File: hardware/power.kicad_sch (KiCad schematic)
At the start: 34 parts, among them U3 TI LMR51430YFDDCR, U4 TI LMR51430YFDDCR, U5 TPS2116DRLR, U6 NCV8187AMT180TAG, U7 LP5912-3.3DRVR

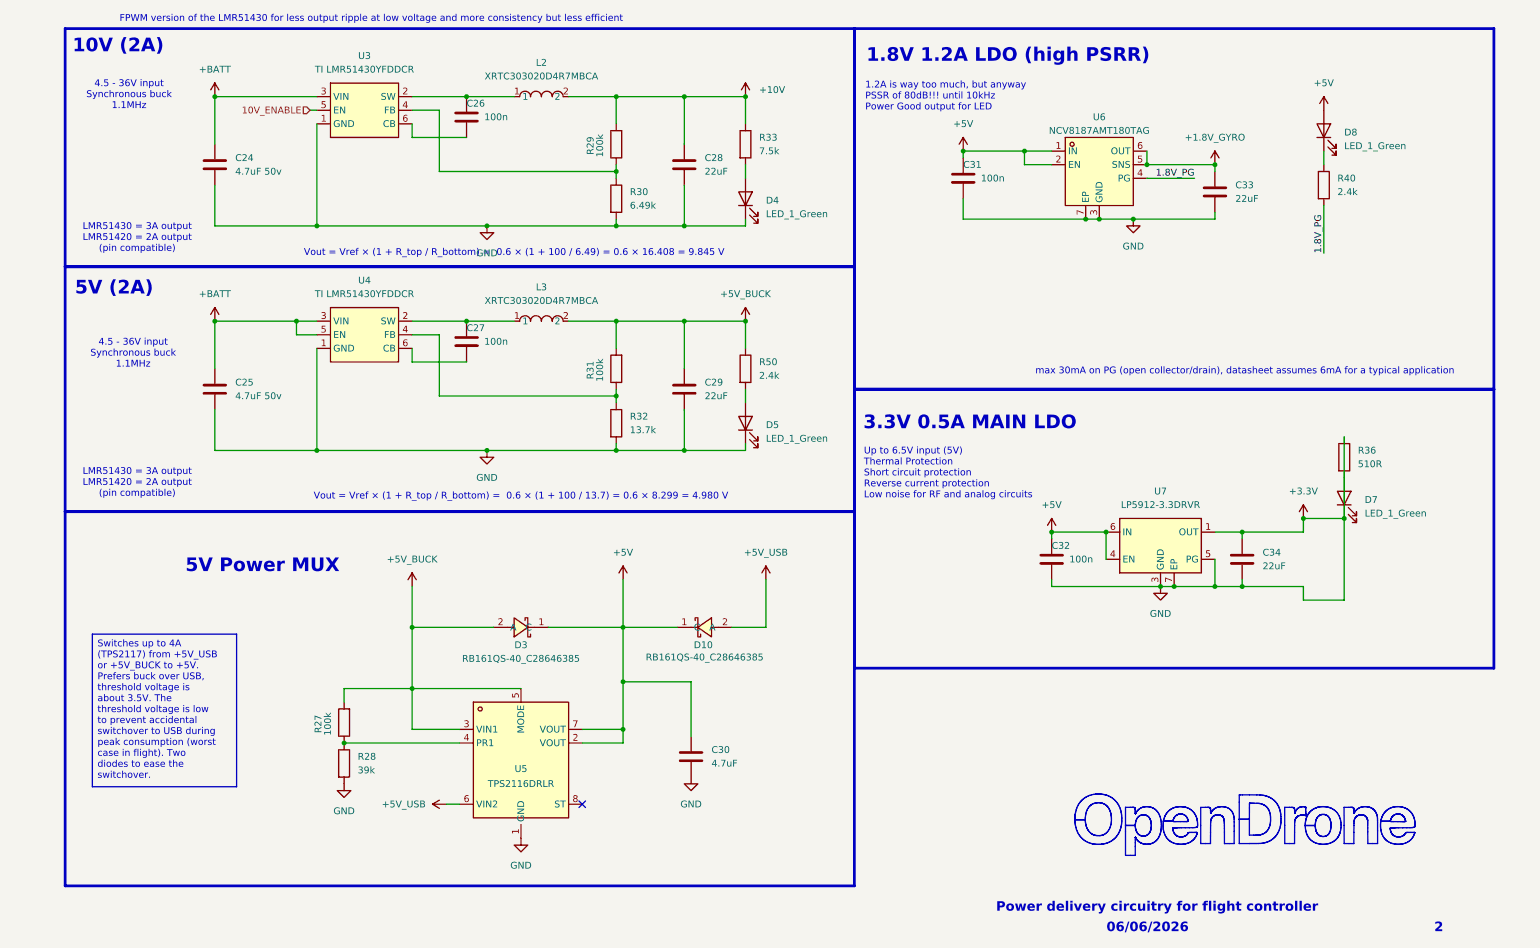
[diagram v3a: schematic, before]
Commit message: fix(power): break accidental +3.3V↔GND short in power sheet
A +3.3V power symbol (#PWR084) and a GND symbol (#PWR068) were tied to the same
net during schematic annotation, merging the entire ground into +3.3V (no GND
net, 14 shorted caps, LDO IN/GND/OUT shorted). Separated them; ERC +3.3V/GND
conflict cleared, GND net restored (91 pins), 0 shorted caps. PCB unaffected.

Co-Authored-By: Claude Opus 4.8 (1M context) <noreply@anthropic.com>
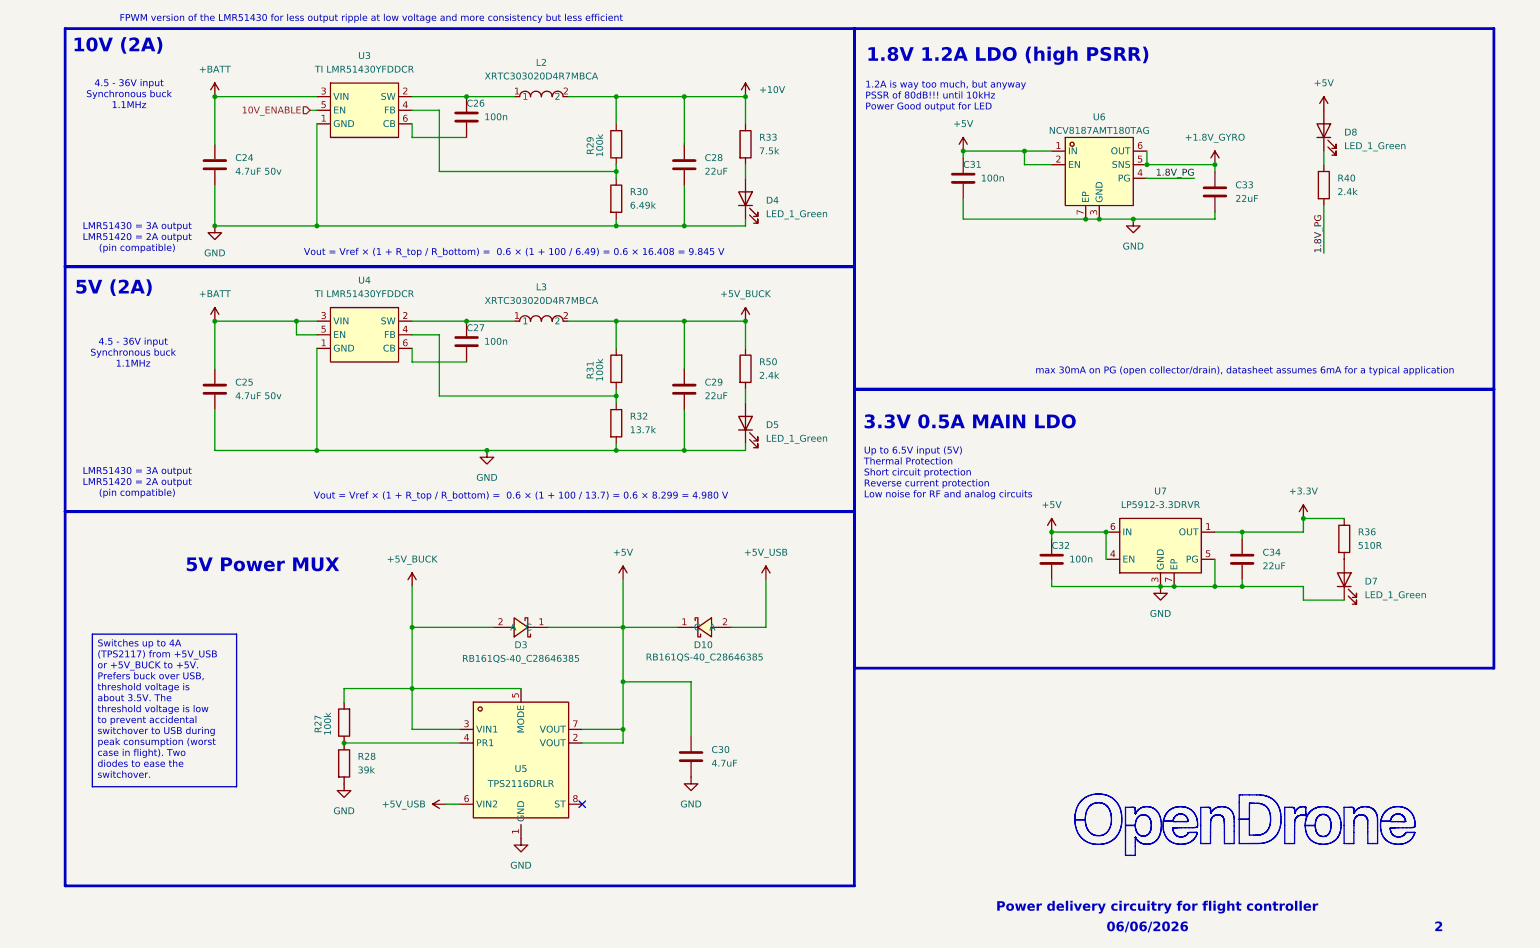
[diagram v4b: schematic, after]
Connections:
- net +3.3V: no longer C24.2, C25.2, C28.2, C29.2, C30.2, C31.2, C32.2, C33.2, C34.2, D4.1 (K), D5.1 (K), D7.1 (K), R28.2, R30.2, R32.2, U3.1 (GND), U4.1 (GND), U5.1 (GND), U6.3 (GND), U6.7 (EP), U7.3 (GND), U7.5 (PG), U7.7 (EP)
- new net GND: C24.2, C25.2, C28.2, C29.2, C30.2, C31.2, C32.2, C33.2, C34.2, D4.1 (K), D5.1 (K), D7.1 (K), R28.2, R30.2, R32.2, U3.1 (GND), U4.1 (GND), U5.1 (GND), U6.3 (GND), U6.7 (EP), U7.3 (GND), U7.5 (PG), U7.7 (EP)
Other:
- moved on the sheet: D7, R36
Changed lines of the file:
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@@
 	)
 	(junction
-		(at 198.12 119.38)
+		(at 245.11 116.84)
 		(diameter 0)
 		(color 0 0 0 0)
 	)
 	(junction
-		(at 245.11 116.84)
+		(at 198.12 119.38)
 		(diameter 0)
 		(color 0 0 0 0)
@@
 	)
 	(junction
-		(at 252.73 116.84)
-		(diameter 0)
-		(color 0 0 0 0)
-	)
-	(junction
 		(at 116.84 104.14)
 		(diameter 0)
@@
 	)
 	(junction
-		(at 118.11 137.16)
+		(at 41.91 62.23)
 		(diameter 0)
 		(color 0 0 0 0)
 	)
 	(junction
-		(at 140.97 38.1)
+		(at 118.11 137.16)
 		(diameter 0)
 		(color 0 0 0 0)
 	)
 	(junction
-		(at 92.71 62.23)
+		(at 140.97 38.1)
 		(diameter 0)
 		(color 0 0 0 0)
@@
 	(wire
 		(pts
-			(xy 213.36 60.96) (xy 228.6 60.96)
+			(xy 245.11 129.54) (xy 245.11 132.08)
 		)
 		(stroke
@@
 	(wire
 		(pts
-			(xy 116.84 80.01) (xy 116.84 85.09)
+			(xy 213.36 60.96) (xy 228.6 60.96)
 		)
 		(stroke
@@
 	(wire
 		(pts
-			(xy 140.97 60.96) (xy 140.97 62.23)
+			(xy 116.84 80.01) (xy 116.84 85.09)
 		)
 		(stroke
@@
 	(wire
 		(pts
-			(xy 218.44 129.54) (xy 220.98 129.54)
+			(xy 140.97 60.96) (xy 140.97 62.23)
 		)
 		(stroke
@@
 	(wire
 		(pts
-			(xy 181.61 48.26) (xy 193.04 48.26)
+			(xy 218.44 129.54) (xy 220.98 129.54)
 		)
 		(stroke
@@
 	(wire
 		(pts
-			(xy 193.04 48.26) (xy 198.12 48.26)
+			(xy 181.61 48.26) (xy 193.04 48.26)
 		)
 		(stroke
@@
 	(wire
 		(pts
-			(xy 110.49 158.75) (xy 118.11 158.75)
+			(xy 193.04 48.26) (xy 198.12 48.26)
 		)
 		(stroke
@@
 	(wire
 		(pts
-			(xy 207.01 60.96) (xy 213.36 60.96)
+			(xy 110.49 158.75) (xy 118.11 158.75)
 		)
 		(stroke
@@
 	(wire
 		(pts
-			(xy 116.84 62.23) (xy 92.71 62.23)
+			(xy 207.01 60.96) (xy 213.36 60.96)
 		)
 		(stroke
@@
 	(wire
 		(pts
-			(xy 60.96 62.23) (xy 41.91 62.23)
+			(xy 41.91 62.23) (xy 116.84 62.23)
 		)
 		(stroke
@@
 	(wire
 		(pts
-			(xy 78.74 148.59) (xy 78.74 156.21)
+			(xy 245.11 116.84) (xy 245.11 119.38)
 		)
 		(stroke
@@
 	(wire
 		(pts
-			(xy 78.74 40.64) (xy 83.82 40.64)
+			(xy 245.11 132.08) (xy 252.73 132.08)
 		)
 		(stroke
@@
 	(wire
 		(pts
-			(xy 41.91 80.01) (xy 41.91 88.9)
+			(xy 78.74 148.59) (xy 78.74 156.21)
 		)
 		(stroke
@@
 	(wire
 		(pts
-			(xy 92.71 104.14) (xy 60.96 104.14)
+			(xy 78.74 40.64) (xy 83.82 40.64)
 		)
 		(stroke
@@
 	(wire
 		(pts
-			(xy 233.68 129.54) (xy 228.6 129.54)
+			(xy 41.91 80.01) (xy 41.91 88.9)
 		)
 		(stroke
@@
 	(wire
 		(pts
-			(xy 92.71 62.23) (xy 60.96 62.23)
+			(xy 92.71 104.14) (xy 60.96 104.14)
 		)
 		(stroke
@@
 	(wire
 		(pts
-			(xy 85.09 170.18) (xy 87.63 170.18)
+			(xy 233.68 129.54) (xy 228.6 129.54)
 		)
 		(stroke
@@
 	(wire
 		(pts
-			(xy 198.12 119.38) (xy 208.28 119.38)
+			(xy 85.09 170.18) (xy 87.63 170.18)
 		)
 		(stroke
@@
 	(wire
 		(pts
-			(xy 116.84 80.01) (xy 129.54 80.01)
+			(xy 198.12 119.38) (xy 208.28 119.38)
 		)
 		(stroke
@@
 	(wire
 		(pts
-			(xy 83.82 82.55) (xy 83.82 93.98)
+			(xy 116.84 80.01) (xy 129.54 80.01)
 		)
 		(stroke
@@
 	(wire
 		(pts
-			(xy 193.04 48.26) (xy 193.04 50.8)
+			(xy 83.82 82.55) (xy 83.82 93.98)
 		)
 		(stroke
@@
 	(wire
 		(pts
-			(xy 78.74 129.54) (xy 78.74 137.16)
+			(xy 193.04 48.26) (xy 193.04 50.8)
 		)
 		(stroke
@@
 	(wire
 		(pts
-			(xy 228.6 124.46) (xy 228.6 129.54)
+			(xy 78.74 129.54) (xy 78.74 137.16)
 		)
 		(stroke
@@
 	(wire
 		(pts
-			(xy 245.11 119.38) (xy 245.11 116.84)
+			(xy 228.6 124.46) (xy 228.6 129.54)
 		)
 		(stroke
@@
 	(wire
 		(pts
-			(xy 252.73 116.84) (xy 252.73 101.6)
-		)
-		(stroke
-			(width 0)
-			(type default)
-		)
-	)
-	(wire
-		(pts
 			(xy 66.04 158.75) (xy 87.63 158.75)
 		)
@@
 	(wire
 		(pts
-			(xy 252.73 132.08) (xy 245.11 132.08)
-		)
-		(stroke
-			(width 0)
-			(type default)
-		)
-	)
-	(wire
-		(pts
 			(xy 248.92 48.26) (xy 248.92 50.8)
 		)
@@
 	(wire
 		(pts
-			(xy 245.11 132.08) (xy 245.11 129.54)
-		)
-		(stroke
-			(width 0)
-			(type default)
-		)
-	)
-	(wire
-		(pts
 			(xy 78.74 82.55) (xy 83.82 82.55)
 		)
@@
 	(wire
 		(pts
-			(xy 252.73 132.08) (xy 252.73 116.84)
+			(xy 118.11 137.16) (xy 118.11 128.27)
 		)
 		(stroke
@@
 	(wire
 		(pts
-			(xy 118.11 137.16) (xy 118.11 128.27)
+			(xy 60.96 82.55) (xy 57.15 82.55)
 		)
 		(stroke
@@
 	(wire
 		(pts
-			(xy 60.96 82.55) (xy 57.15 82.55)
+			(xy 60.96 43.18) (xy 60.96 62.23)
 		)
 		(stroke
@@
 	(wire
 		(pts
-			(xy 60.96 43.18) (xy 60.96 62.23)
+			(xy 99.06 148.59) (xy 78.74 148.59)
 		)
 		(stroke
@@
 	(wire
 		(pts
-			(xy 99.06 148.59) (xy 78.74 148.59)
+			(xy 129.54 62.23) (xy 140.97 62.23)
 		)
 		(stroke
@@
 	(wire
 		(pts
-			(xy 129.54 62.23) (xy 140.97 62.23)
+			(xy 245.11 116.84) (xy 252.73 116.84)
 		)
 		(stroke
@@
 	(wire
 		(pts
-			(xy 245.11 116.84) (xy 252.73 116.84)
-		)
-		(stroke
-			(width 0)
-			(type default)
-		)
-	)
-	(wire
-		(pts
 			(xy 118.11 156.21) (xy 118.11 158.75)
 		)
@@
 	(symbol
 		(lib_id "power:GND")
-		(at 92.71 62.23 0)
+		(at 41.91 62.23 0)
 		(unit 1)
 		(body_style 1)
@@
 		(fields_autoplaced yes)
 		(property "Reference" "#PWR068"
-			(at 92.71 68.58 0)
+			(at 41.91 68.58 0)
 			(hide yes)
 			(show_name no)
@@
 		)
 		(property "Value" "GND"
-			(at 92.71 67.31 0)
+			(at 41.91 67.31 0)
 			(show_name no)
 			(do_not_autoplace no)
@@
 		)
 		(property "Footprint" ""
-			(at 92.71 62.23 0)
+			(at 41.91 62.23 0)
 			(hide yes)
 			(show_name no)
@@
 		)
 		(property "Datasheet" ""
-			(at 92.71 62.23 0)
+			(at 41.91 62.23 0)
 			(hide yes)
 			(show_name no)
@@
 		)
 		(property "Description" "Power symbol creates a global label with name \"GND\" , ground"
-			(at 92.71 62.23 0)
+			(at 41.91 62.23 0)
 			(hide yes)
 			(show_name no)
@@
 	(symbol
 		(lib_id "Device:LED")
-		(at 252.73 113.03 90)
+		(at 252.73 128.27 90)
 		(unit 1)
 		(body_style 1)
@@
 		(fields_autoplaced yes)
 		(property "Reference" "D7"
-			(at 256.54 113.3474 90)
+			(at 256.54 128.5874 90)
 			(show_name no)
 			(do_not_autoplace no)
@@
 		)
 		(property "Value" "LED_1_Green"
-			(at 256.54 115.8874 90)
+			(at 256.54 131.1274 90)
 			(show_name no)
 			(do_not_autoplace no)
@@
 		)
 		(property "Footprint" "LED_SMD:LED_0402_1005Metric"
-			(at 252.73 113.03 0)
+			(at 252.73 128.27 0)
 			(hide yes)
 			(show_name no)
@@
 		)
 		(property "Datasheet" ""
-			(at 252.73 113.03 0)
+			(at 252.73 128.27 0)
 			(hide yes)
 			(show_name no)
@@
 		)
 		(property "Description" ""
-			(at 252.73 113.03 0)
+			(at 252.73 128.27 0)
 			(hide yes)
 			(show_name no)
@@
 		)
 		(property "LCSC" "C965793"
-			(at 252.73 113.03 90)
+			(at 252.73 128.27 90)
 			(hide yes)
 			(show_name no)
@@
 		)
 		(property "MPN" "XL-1005UGC "
-			(at -54.61 43.18 0)
+			(at -54.61 58.42 0)
 			(hide yes)
 			(show_name no)
@@
 		)
 		(property "Manufacturer" "XINGLIGHT"
-			(at -54.61 43.18 0)
+			(at -54.61 58.42 0)
 			(hide yes)
 			(show_name no)
@@
 	(symbol
 		(lib_id "Device:R")
-		(at 252.73 105.41 0)
+		(at 252.73 120.65 0)
 		(unit 1)
 		(body_style 1)
@@
 		(fields_autoplaced yes)
 		(property "Reference" "R36"
-			(at 255.27 104.1399 0)
+			(at 255.27 119.3799 0)
 			(show_name no)
 			(do_not_autoplace no)
@@
 		)
 		(property "Value" "510R"
-			(at 255.27 106.6799 0)
+			(at 255.27 121.9199 0)
 			(show_name no)
 			(do_not_autoplace no)
@@
 		)
 		(property "Footprint" "Resistor_SMD:R_0201_0603Metric"
-			(at 250.952 105.41 90)
+			(at 250.952 120.65 90)
 			(hide yes)
 			(show_name no)
@@
 		)
 		(property "Datasheet" ""
-			(at 252.73 105.41 0)
+			(at 252.73 120.65 0)
 			(hide yes)
 			(show_name no)
@@
 		)
 		(property "Description" "Resistor"
-			(at 252.73 105.41 0)
+			(at 252.73 120.65 0)
 			(hide yes)
 			(show_name no)
@@
 		)
 		(property "LCSC" "C57784"
-			(at 252.73 105.41 0)
+			(at 252.73 120.65 0)
 			(hide yes)
 			(show_name no)
@@
 		)
 		(property "MPN" ""
-			(at 0 1.27 0)
+			(at 0 16.51 0)
 			(hide yes)
 			(show_name no)
@@
 		)
 		(property "Manufacturer" ""
-			(at 0 1.27 0)
+			(at 0 16.51 0)
 			(hide yes)
 			(show_name no)

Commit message: Swap 1.8V LDO and IMU, fix BOM/CPL export hygiene
Part changes, both schematic and PCB:
- U6 NCV8187AMT180TAG (stock 0 at JLC) replaced by U12 LP5912-1.8DRVR
  (C2876234). Same WSON-6 2x2 land pattern as the LP5912-3.3 at U7, so no
  layout change. PG is retained. PSRR at the 1 mA gyro load is ~85 dB to
  1 kHz and ~70 dB at 10 kHz per datasheet Figure 23.
- PG indicator rewired: pull-up from +5V to PG, LED from PG to GND, so the
  LED lights when the rail is good instead of when it has failed.
- U9 LSM6DSV16XTR replaced by BMI270 (C2836813). Bosch Table 22 matches the
  existing LGA-14 symbol pin for pin, so no rewire and no CPL rotation change.
- C33, C34 22uF 0402 moved from C105226 to C415703.

Export fixes:
- U12 carried its part number in a field named "LCSC Part" rather than
  "LCSC", so it exported with no part number and would have been quoted
  unsourced. Renamed.
- The 34 solder pad and testpoint footprints now carry exclude_from_bom
  plus exclude_from_pos_files instead of relying on the dnp flag. They stay
  on the board as copper but no longer need --exclude-dnp at export time.

BOM and CPL now agree at 101 placements with no blank part numbers, exported
without any dnp flag. ERC is unchanged against HEAD (170 vs 171 violations,
all pre-existing).

Co-Authored-By: Claude Fable 5 <noreply@anthropic.com>
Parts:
- removed R40: 2.4k, Resistor_SMD:R_0201_0603Metric, symbol Device:R
- removed U6: NCV8187AMT180TAG, lib:WDFN-6_L2.0-W2.0-P0.65-BL-EP, symbol lib:NCV8187AMT180TAG
- added R34: 6.49k, Resistor_SMD:R_0201_0603Metric, symbol Device:R
- added U12: LP5912-1.8DRVR, lib:WSON-6-1EP_2x2mm_P0.65mm_EP1x1.6mm_ThermalVias, symbol lib:LP5912-1.8DRVR
- C31: value 100n -> 4.7uF; footprint Capacitor_SMD:C_0201_0603Metric -> Capacitor_SMD:C_0402_1005Metric; LCSC C76939 -> C23733; MPN GRM033R61E104KE14D -> CL05A475MP5NRNC; Manufacturer Murata Electronics -> Samsung Electro-Mechanics
- C33, C34: LCSC C105226 -> C415703; MPN CL05A226MQ5QUNC -> GRM155R60J226ME11D; Manufacturer Samsung Electro-Mechanics -> Murata
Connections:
- net +1.8V_GYRO: now also U12.1 (OUT)
- net +5V: now also R34.1, U12.4 (EN), U12.6 (IN); no longer D8.2 (A)
- net 1.8V_PG: now also D8.2 (A), R34.2, U12.3 (PG)
- net GND: now also D8.1 (K), U12.5 (GND), U12.7 (EP)
- no-connect marks 1 -> 2
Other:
- note added: "1.8V LDO for IMU (high PSRR)"
- note removed: "1.2A is way too much, but anyway PSSR of 80dB!!! until 10kHz Power Good output for LED"
- note removed: "1.8V 1.2A LDO (high PSRR)"
- note removed: "max 30mA on PG (open collector/drain), datasheet assumes 6mA for a typical application"
- moved on the sheet: C33, D8

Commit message: Rev 3: LP5912 gyro LDO, BMI270
Gyro supply moves to LP5912-1.8DRVR (U12, C2876234); the NCV8187AMT180TAG is
gone from schematic and board. IMU is BMI270 (U9). Bucks stay LMR51430YFDDCR,
which has adequate margin for the 6S ceiling this board shares with the 20x20
ESC.

ERC and DRC reviewed by the maintainer.

Co-Authored-By: Claude Opus 5 (1M context) <noreply@anthropic.com>
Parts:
- U3, U4: value TI LMR51430YFDDCR -> LMR51430YFDDCR; MPN TI LMR51430YFDDCR -> LMR51430YFDDCR
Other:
- note added: "10V (3A)"
- note added: "5V (3A)"
- note removed: "10V (2A)"
- note removed: "5V (2A)"

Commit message: 4V5 rework: TPS2116 mux replaced by DSK24 diode-OR
U5, its diodes, R27/R28 and C30 removed. D6 from the buck output and
D10 from +5V_USB feed the new +4v5 net for the LDOs, JST and pads; the
buck output is plain +5V to the external pads. DSK24 footprint and 3D
model committed with the change. Shop badge gold.

Co-Authored-By: Claude Opus 5 (1M context) <noreply@anthropic.com>
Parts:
- removed C30: 4.7uF, Capacitor_SMD:C_0402_1005Metric, symbol Device:C
- removed D10, D3: RB161QS-40_C28646385, lib:SOD-882_L1.0-W0.6-RD, symbol lib:RB161QS-40_C28646385
- removed R27: 100k, Resistor_SMD:R_0201_0603Metric, symbol Device:R
- removed R28: 39k, Resistor_SMD:R_0201_0603Metric, symbol Device:R
- removed U5: TPS2116DRLR, lib:SOT-583-8_L2.1-W1.6-P0.50-LS1.6-BL, symbol lib:TPS2116DRLR
- added D10, D6: DSK24, lib:SOD-123_L2.8-W1.8-LS3.7-RD, symbol lib:DSK24_C64890
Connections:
- net +5V_BUCK is gone; now on net +5V: C29.1, L3.2, R31.2, R50.1
- net +5V: now also D6.2 (A); no longer C31.1, C32.1, R34.1, U12.4 (EN), U12.6 (IN), U7.4 (EN), U7.6 (IN)
- net +5V_USB: now also D10.2 (A)
- new net +4v5: C31.1, C32.1, D10.1 (K), D6.1 (K), R34.1, U12.4 (EN), U12.6 (IN), U7.4 (EN), U7.6 (IN)
- no-connect marks 2 -> 1

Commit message: schematics: complete Manufacturer/MPN coverage, trim stray whitespace
22 field fixes across blackbox, osd, power, rp2350a: Manufacturer backfilled
from the LCSC catalogue, trailing space trimmed from four XL-1005UGC MPNs.
pads.kicad_sch (uncommitted WIP) untouched. Part of the fab-agnostic BOM
standardisation for quoting outside JLCPCB.

kicad-skip reflowed the touched files; structural diff shows only property
changes, ERC identical (163 violations before and after).

Co-Authored-By: Claude Fable 5 <noreply@anthropic.com>
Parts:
- D4, D5, D7, D8: MPN XL-1005UGC -> XL-1005UGC
- R30, R34: MPN (none) -> AF0201FR-076K49L; Manufacturer (none) -> YAGEO
- R33: MPN (none) -> RC0201FR-077K5L; Manufacturer (none) -> YAGEO
- R36: MPN (none) -> RC0201FR-07510RL; Manufacturer (none) -> YAGEO
- R50: MPN (none) -> RTT012401FTH; Manufacturer (none) -> RALEC
